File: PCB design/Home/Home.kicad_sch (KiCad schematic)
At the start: 15 parts, among them J1 Fan, J2 LCD, J3 EM LOCK, J4 ACS712 Signal, J5 Power In, J6 ACS712 Power, U1 ESP32-WROOM-32, U3 DHT11, U7 LM2596S-ADJ, U8 LM2596S-ADJ

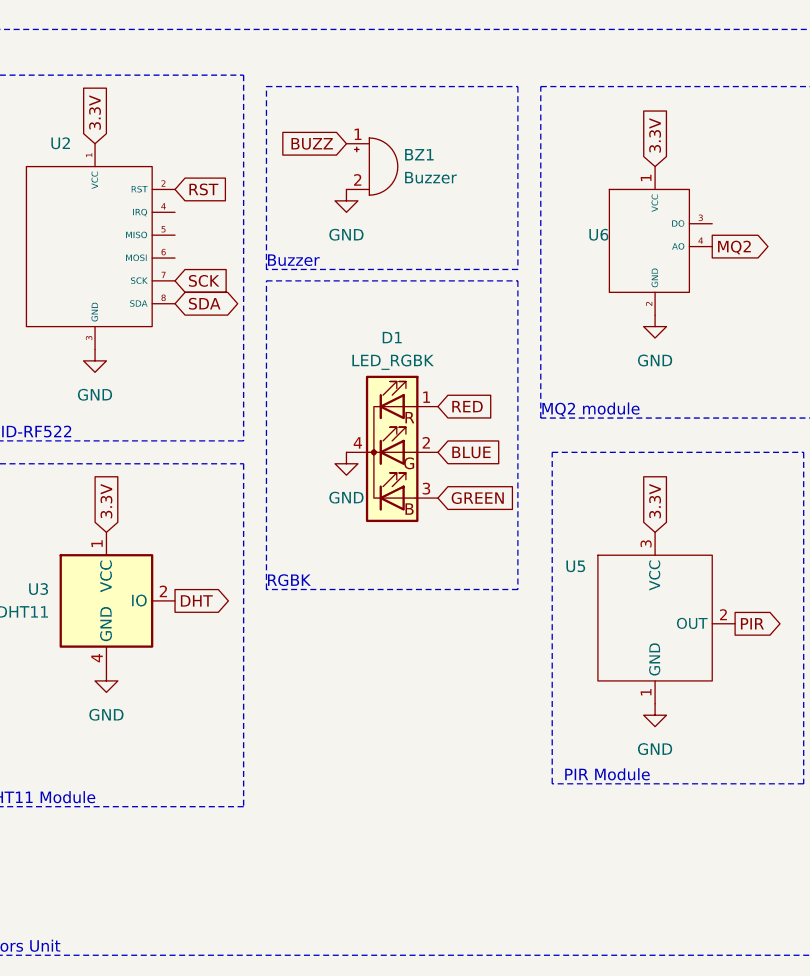
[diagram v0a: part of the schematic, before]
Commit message: added ACS sensor
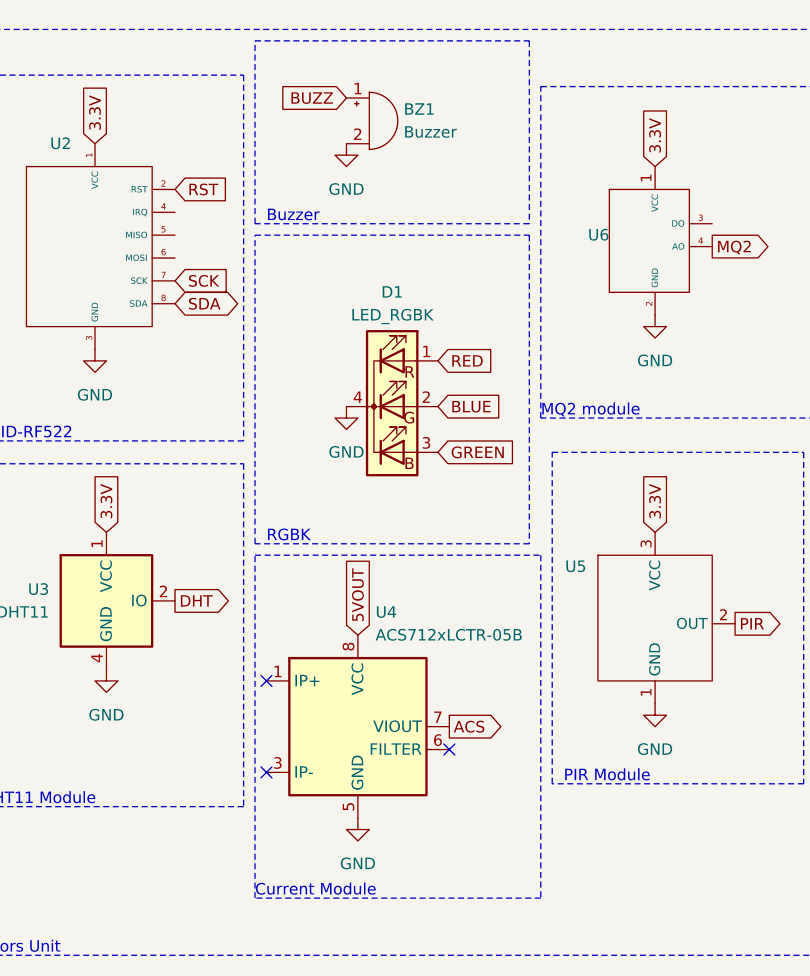
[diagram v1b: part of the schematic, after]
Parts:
- added U4: ACS712xLCTR-05B, Package_SO:SOIC-8_3.9x4.9mm_P1.27mm, symbol Sensor_Current:ACS712xLCTR-05B
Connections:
- net 5VOUT: now also U4.8 (VCC)
- net ACS: now also U4.7 (VIOUT)
- net GND: now also U4.5 (GND)
- new net: U4.1 (IP+), U4.2 (IP+)
- new net: U4.3 (IP-), U4.4 (IP-)
- no-connect marks 17 -> 20
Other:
- note added: "Current Module"
- moved on the sheet: BZ1, D1
